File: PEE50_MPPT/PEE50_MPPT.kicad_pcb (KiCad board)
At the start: 2 copper layers, 125 x 125 mm, 172 parts, among them J1 Vout, J2 Conn_01x02_Female, J3 Conn_01x02_Female, J4 Conn_01x03_Female, J5 PV_IN1, J6 PV_IN1, J7 PV_IN1, J8 PV_IN1, Q1 BC547, Q2 BC547, Q3 BC547, Q4 BC547, U1 LM3480-3.3, U10 NTA4151PT1G, U11 CSD18514Q5A, U12 CSD18543Q3A, U13 TPS552882QRPMRQ1, U14 MAX44284FAUT+T, U15 MAX44284FAUT+T, U16 NTA4151PT1G, U17 CSD18514Q5A, U18 CSD18543Q3A, U19 TPS552882QRPMRQ1, U2 MSP430FR2353TDBT, U20 MAX44284FAUT+T, U21 MAX44284FAUT+T, U22 NTA4151PT1G, U23 CSD18514Q5A, U24 CSD18543Q3A, U25 TPS552882QRPMRQ1, U26 MAX44284FAUT+T, U27 MAX44284FAUT+T, U3 ADG706BRUZ, U4 NTA4151PT1G, U5 CSD18514Q5A, U6 CSD18543Q3A, U7 TPS552882QRPMRQ1, U8 MAX44284FAUT+T, U9 MAX44284FAUT+T

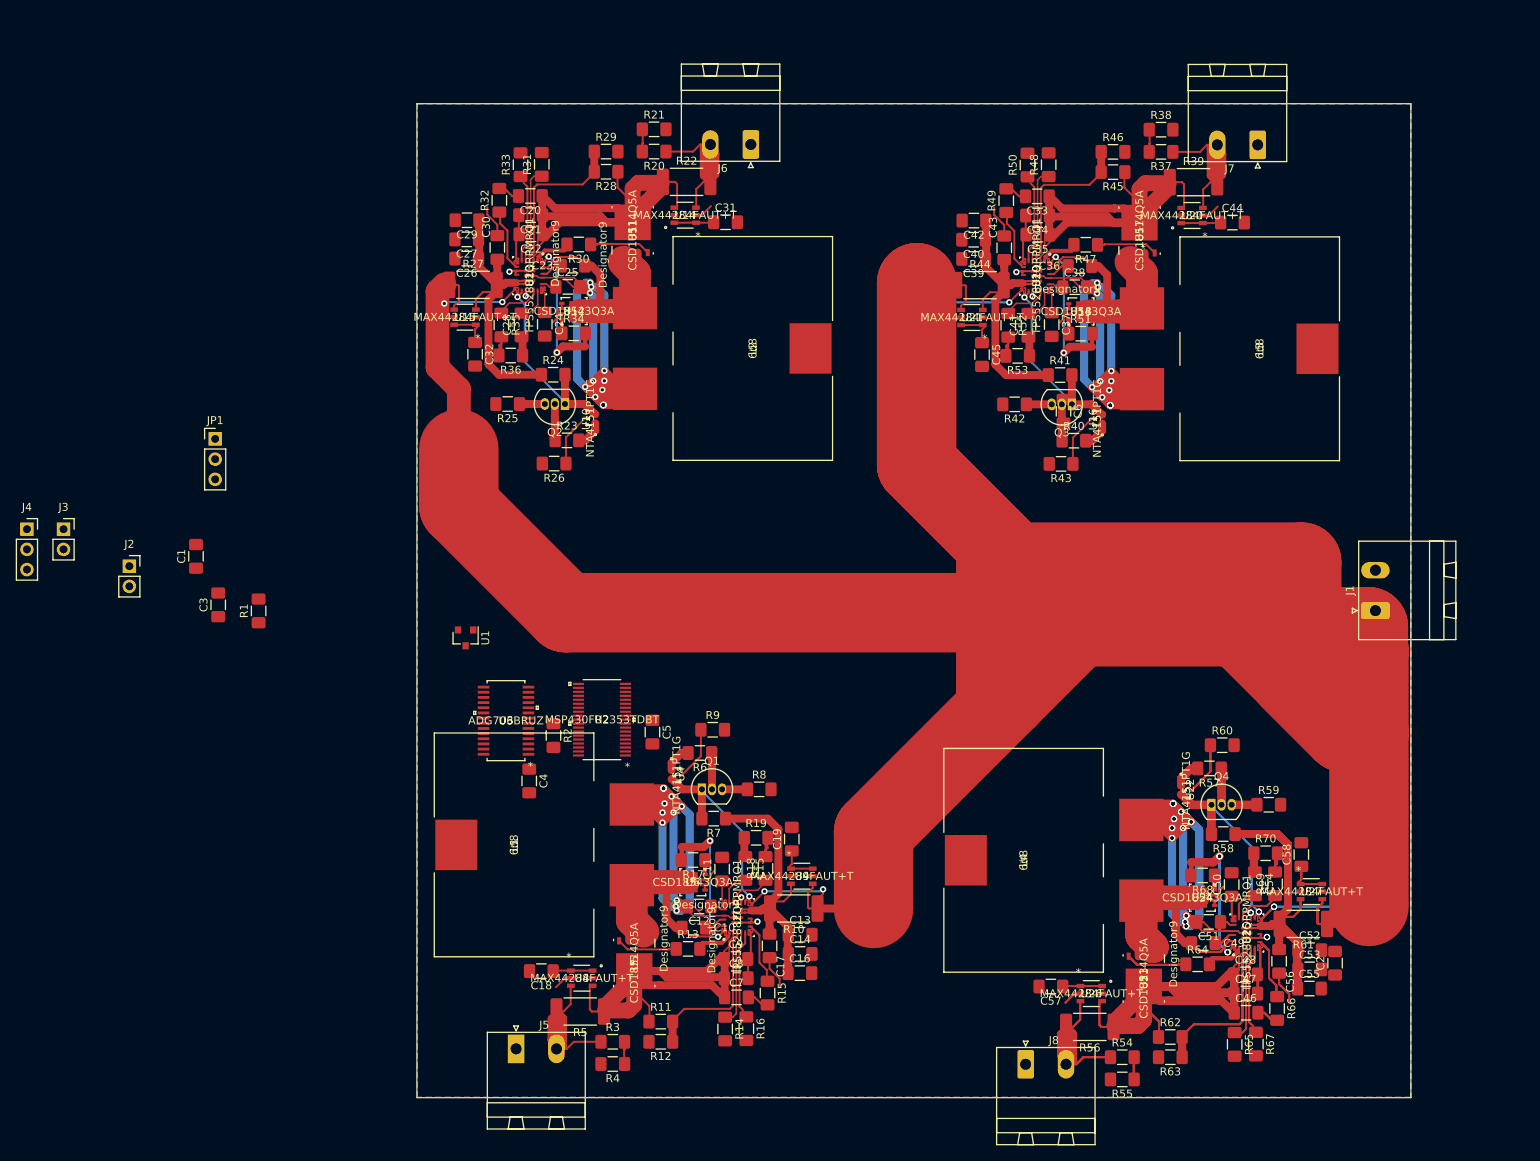
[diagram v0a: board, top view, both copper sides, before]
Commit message: spinneweb aangemaakt
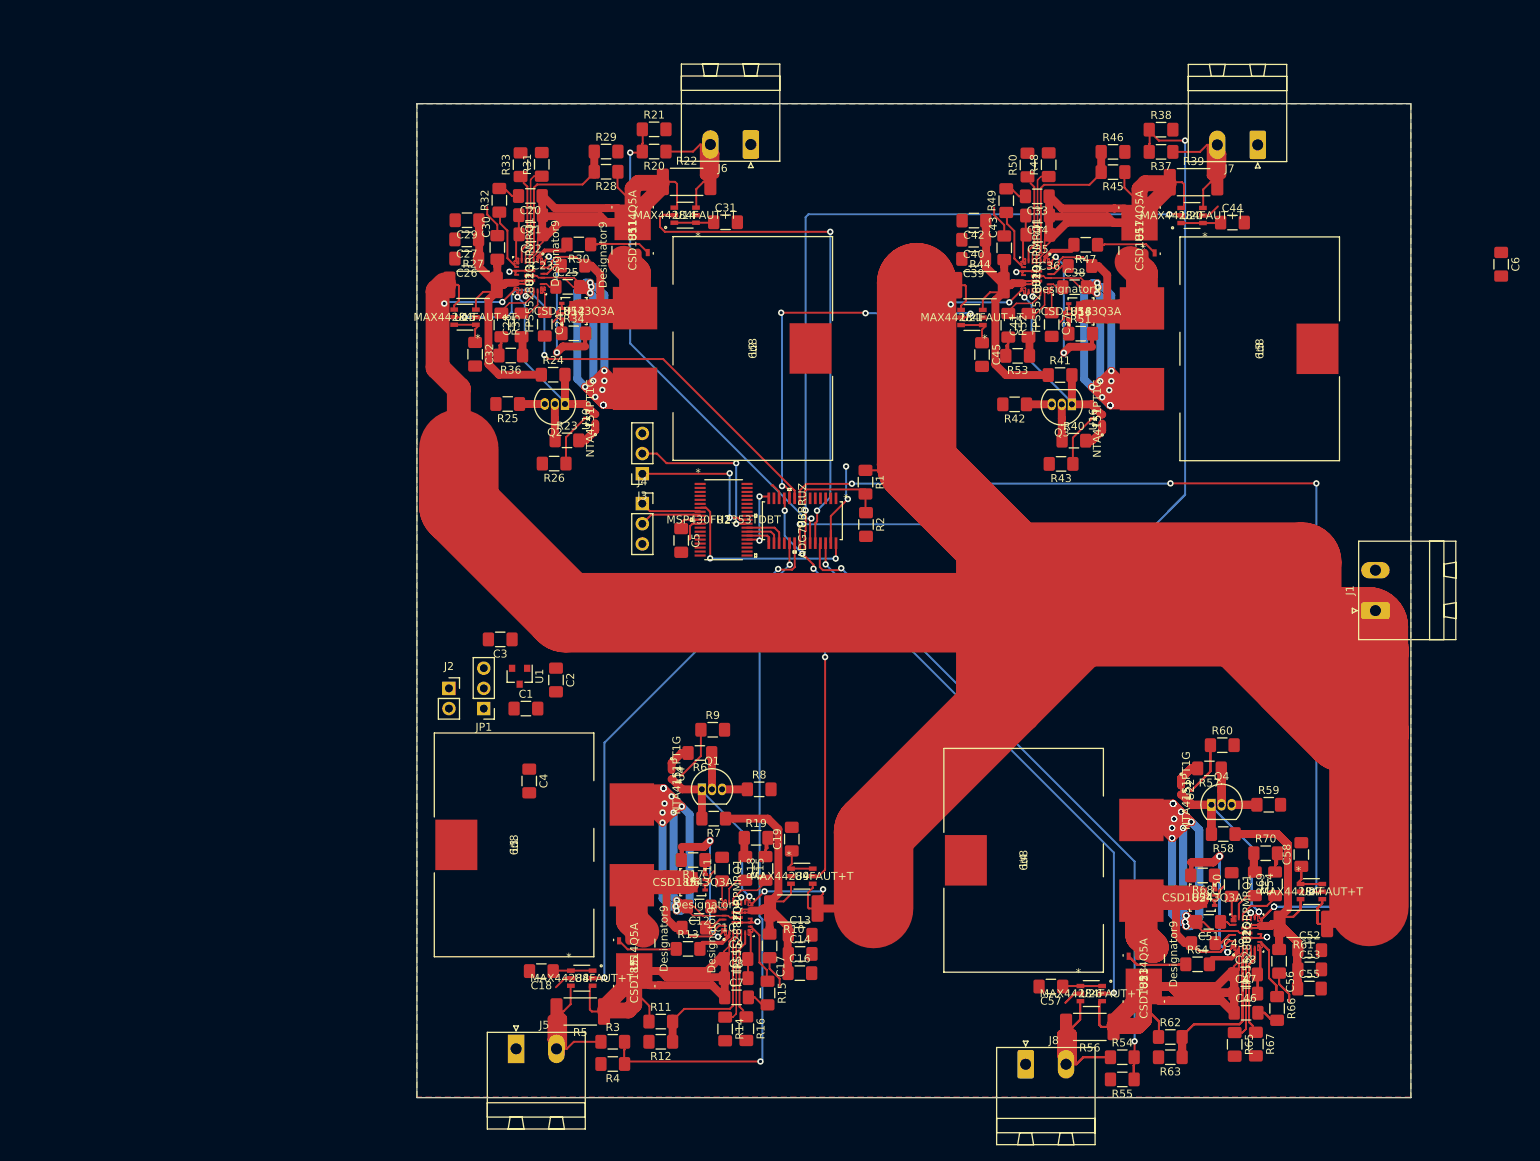
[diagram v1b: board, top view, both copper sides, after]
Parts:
- J3: value Conn_01x02_Female -> Conn_01x03_Female; footprint Connector_PinSocket_2.54mm:PinSocket_1x02_P2.54mm_Vertical -> Connector_PinSocket_2.54mm:PinSocket_1x03_P2.54mm_Vertical
- moved C2 104.3 mm to (42.5, 127.5), turned to 270 degrees
- moved R1 78.0 mm to (81.4, 102.6), turned to 270 degrees
- moved J4 77.5 mm to (53.3, 105.3)
- moved J3 73.1 mm to (53.3, 101.5), turned to 180 degrees
- moved C6 58.1 mm to (161.4, 75.2)
- moved JP1 47.9 mm to (33.4, 131.1), turned to 180 degrees
- moved R2 47.4 mm to (81.5, 107.9)
- moved C1 45.7 mm to (38.7, 131.1), turned to 0 degrees
- moved U3 45.0 mm to (73.5, 107.4), turned to 270 degrees
- moved J2 43.0 mm to (29.0, 128.5)
- moved C3 35.7 mm to (35.5, 122.4), turned to 180 degrees
- moved U2 29.4 mm to (63.6, 107.3), turned to 0 degrees
- moved C5 24.4 mm to (58.2, 109.9)
- moved U1 8.33 mm to (37.9, 127.0)
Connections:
- C5 pad 1: Net-(C5-Pad1) -> +3V3
- R20 pad 2: Vpv1 -> Vpv3
- R21 pad 1: Vpv1 -> Vpv3
- R23 pad 2: DAC1 -> DAC3
- R37 pad 2: Vpv1 -> Vpv2
- R38 pad 1: Vpv1 -> Vpv2
- R40 pad 2: DAC1 -> DAC2
- R54 pad 2: Vpv1 -> Vpv4
- R55 pad 1: Vpv1 -> Vpv4
- R57 pad 2: DAC1 -> DAC4
- U10 pad 1: DAC1 -> DAC3
- U14 pad 5: Ipv1 -> Ipv3
- U15 pad 5: Imppt1 -> Imppt3
- U16 pad 1: DAC1 -> DAC2
- U2 pad 10: Net-(C5-Pad1) -> +3V3
- U2 pad 2: (no net) -> DAC3
- U2 pad 30: (no net) -> DAC2
- U2 pad 34: (no net) -> DAC4
- U20 pad 5: Ipv1 -> Ipv2
- U21 pad 5: Imppt1 -> Imppt2
- U22 pad 1: DAC1 -> DAC4
- U26 pad 5: Ipv1 -> Ipv4
- U27 pad 5: Imppt1 -> Imppt4
- U3 pad 10: (no net) -> Imppt2
- U3 pad 21: (no net) -> Vpv2
- U3 pad 22: (no net) -> Ipv2
- U3 pad 23: (no net) -> Vpv3
- U3 pad 24: (no net) -> Ipv3
- U3 pad 25: (no net) -> Vpv4
- U3 pad 26: (no net) -> Ipv4
- U3 pad 8: (no net) -> Imppt4
- U3 pad 9: (no net) -> Imppt3
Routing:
- net Imppt4: track 0.00 -> 119.4 mm, vias 0 -> 4
- net Vpv2: track 0.00 -> 107.5 mm, vias 0 -> 2
- net Ipv2: track 0.00 -> 90.0 mm, vias 0 -> 2
- net Vpv4: track 0.00 -> 88.7 mm, vias 0 -> 2
- net Ipv4: track 0.00 -> 73.0 mm, vias 0 -> 2
- net Vpv1: track 14.7 -> 86.9 mm, vias 0 -> 2
- net Ipv1: track 0.00 -> 67.3 mm, vias 0 -> 2
- net Ipv3: track 0.00 -> 64.9 mm, vias 0 -> 2
- net Vpv3: track 0.00 -> 63.4 mm, vias 0 -> 2
- net Imppt3: track 0.00 -> 60.7 mm, vias 0 -> 2
- net Imppt1: track 0.00 -> 50.9 mm, vias 0 -> 4
- net Imppt2: track 0.00 -> 48.8 mm, vias 0 -> 4
- net /uC_MPPT/ADC: track 0.00 -> 25.0 mm, vias 0 -> 2
- net Net-(J3-Pad2): track 0.00 -> 21.0 mm, vias 0 -> 2
- net Net-(J3-Pad1): track 0.00 -> 19.1 mm, vias 0 -> 2
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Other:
- net class power: trace_width 10 -> 0.25

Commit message: pff alles verbonden maar veel errors
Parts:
- moved C6 85.5 mm to (81.1, 104.7), turned to 0 degrees
- moved C4 14.4 mm to (46.2, 127.6)
- moved R1 10.3 mm to (86.7, 111.5), turned to 180 degrees
- moved R2 2.31 mm to (82.4, 110.0), turned to 90 degrees
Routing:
- net +3V3: track 52.2 -> 517.9 mm, vias 0 -> 13
- net DAC4: track 6.98 -> 83.8 mm, vias 0 -> 2
- net DAC2: track 3.49 -> 51.7 mm, vias 0 -> 2
- net DAC1: track 3.49 -> 43.7 mm, vias 0 -> 2
- net Vpv1: track 86.9 -> 125.2 mm
- net Pgnd: track 150.5 -> 184.3 mm, vias 12 -> 24
- net Vpv4: track 88.7 -> 112.5 mm
- net DAC3: track 3.49 -> 23.3 mm
- net Vpv3: track 63.4 -> 77.5 mm
- net Vpv2: track 107.5 -> 96.5 mm
- net Vout: track 11.5 -> 19.7 mm, vias 0 -> 2
- net Net-(C3-Pad1): track 0.00 -> 7.32 mm
- net Ipv1: track 67.3 -> 73.8 mm
- net (no net): track 0.00 -> 5.88 mm
- net Imppt3: track 60.7 -> 54.9 mm
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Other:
- outline, holes or cut-outs redrawn

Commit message: gerber gegenereerd om te testen, begonnen aan silkscreen fixen
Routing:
- net Vpv1: track 125.2 -> 88.7 mm
- net Ipv1: track 73.8 -> 77.4 mm
- net +3V3: track 517.9 -> 517.3 mm
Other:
- outline, holes or cut-outs redrawn
- net class power: trace_width 0.25 -> 8
- board text added: "+"
- board text added: "-"
- board text added: "GND"
- board text added: "RST"
- board text added: "RX"
- board text added: "TEST"
- board text added: "TX"
- board text added: "Vout"

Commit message: heel wat silkscreen gefixt
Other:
- board text added: "1"

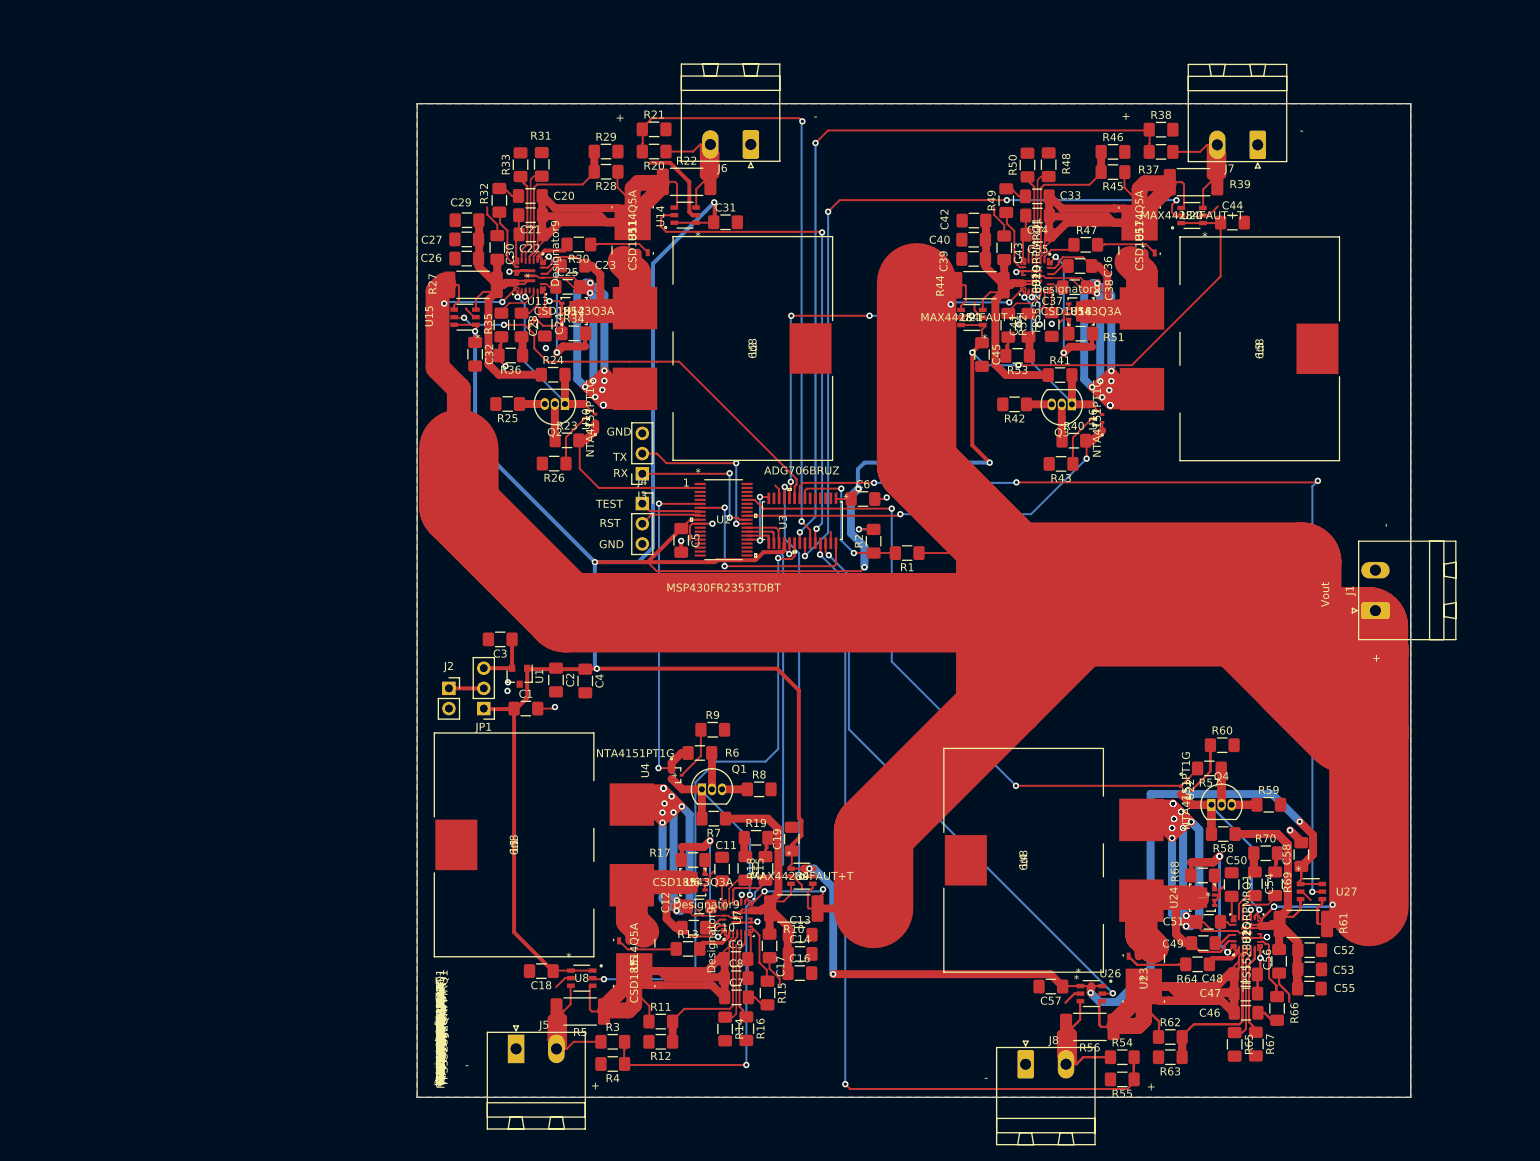
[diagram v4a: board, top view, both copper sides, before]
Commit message: reset pin en errors weggewerkt
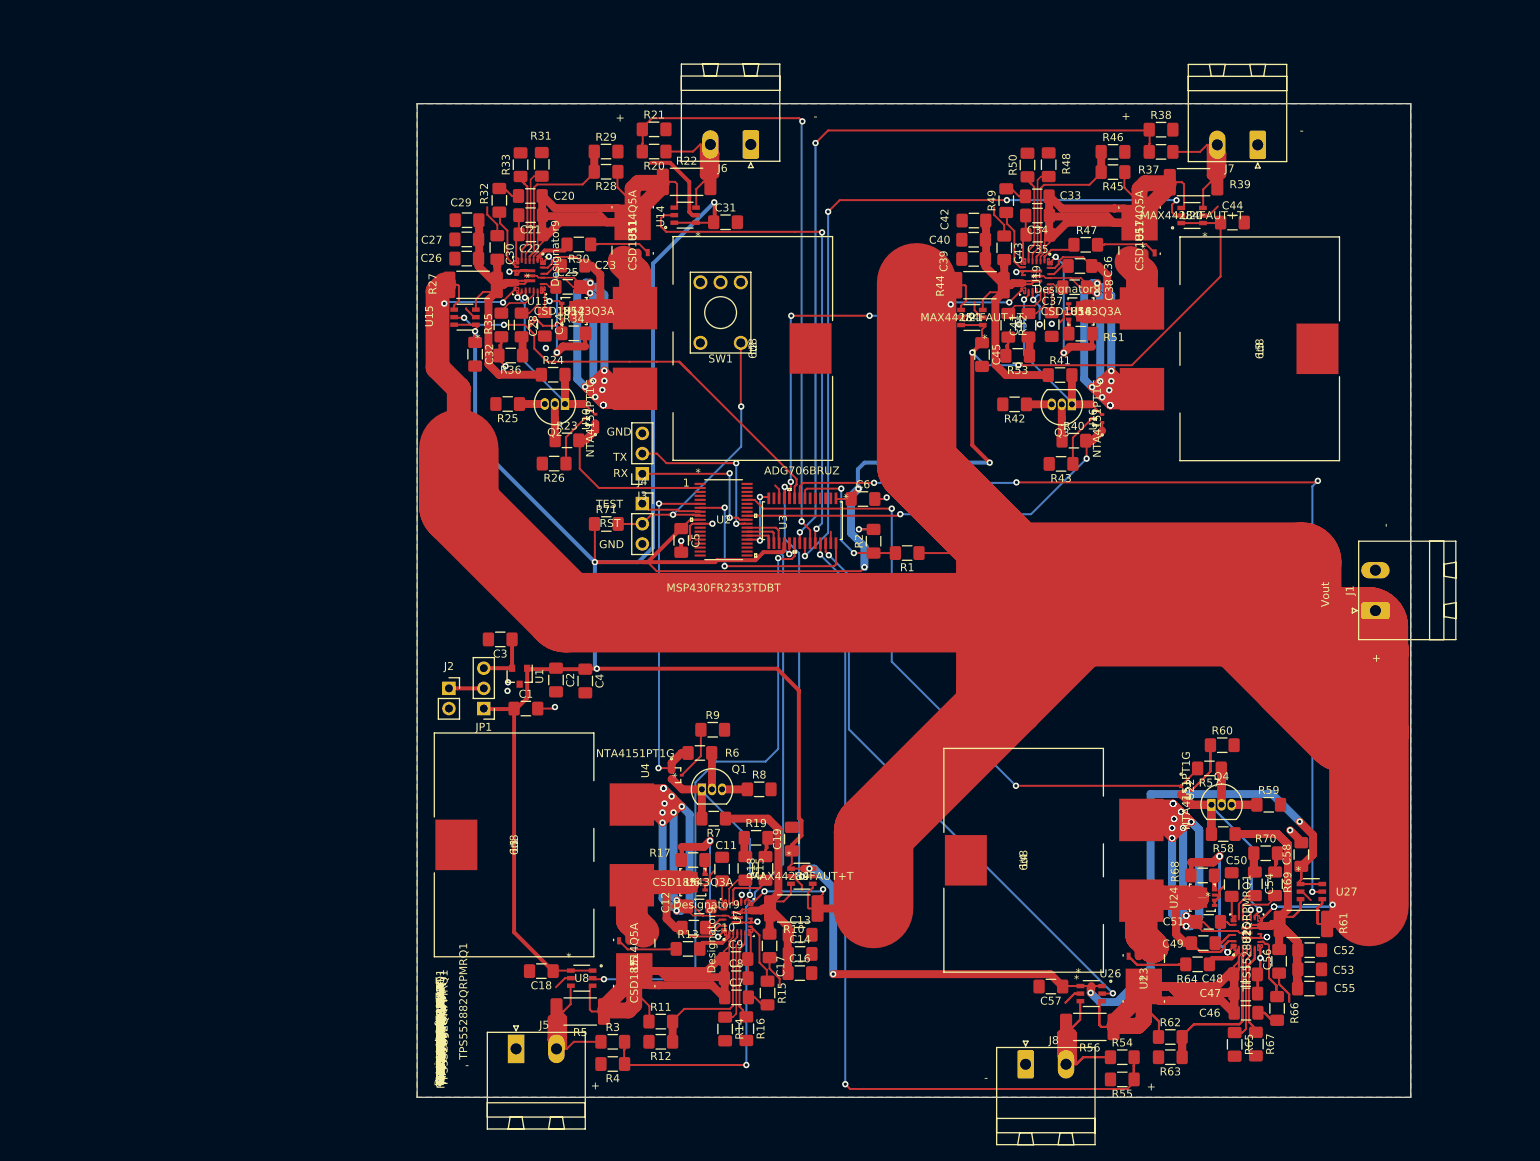
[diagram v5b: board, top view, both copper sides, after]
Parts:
- added R71: 10k, Resistor_SMD:R_1206_3216Metric_Pad1.42x1.75mm_HandSolder, F.Cu at (48.8, 107.8)
- added SW1: SW_DIP_x01, Button_Switch_THT:KSA_Tactile_SPST, F.Cu at (65.7, 85.1)
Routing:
- net Net-(J4-Pad2): track 7.71 -> 36.5 mm, vias 0 -> 2
- net +3V3: track 517.3 -> 522.4 mm
- net Imppt3: track 54.9 -> 57.0 mm
- net Pgnd: track 184.3 -> 182.6 mm
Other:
- net class Default: clearance 0.2 -> 0.1
- rule trace_clearance: 0.2 -> 0.1

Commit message: reset knop op goede plek neergezet
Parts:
- moved SW1 49.7 mm to (68.1, 134.7), turned to 90 degrees
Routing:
- net Net-(J4-Pad2): track 36.5 -> 70.9 mm
- net Vpv4: track 112.5 -> 106.1 mm
- net Vpv2: track 96.5 -> 91.9 mm
- net Vpv3: track 77.5 -> 73.6 mm
- net Pgnd: track 182.6 -> 183.9 mm
